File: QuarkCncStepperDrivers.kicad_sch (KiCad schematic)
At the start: 2 parts, among them J1 Conn_01x14, J2 Conn_01x14

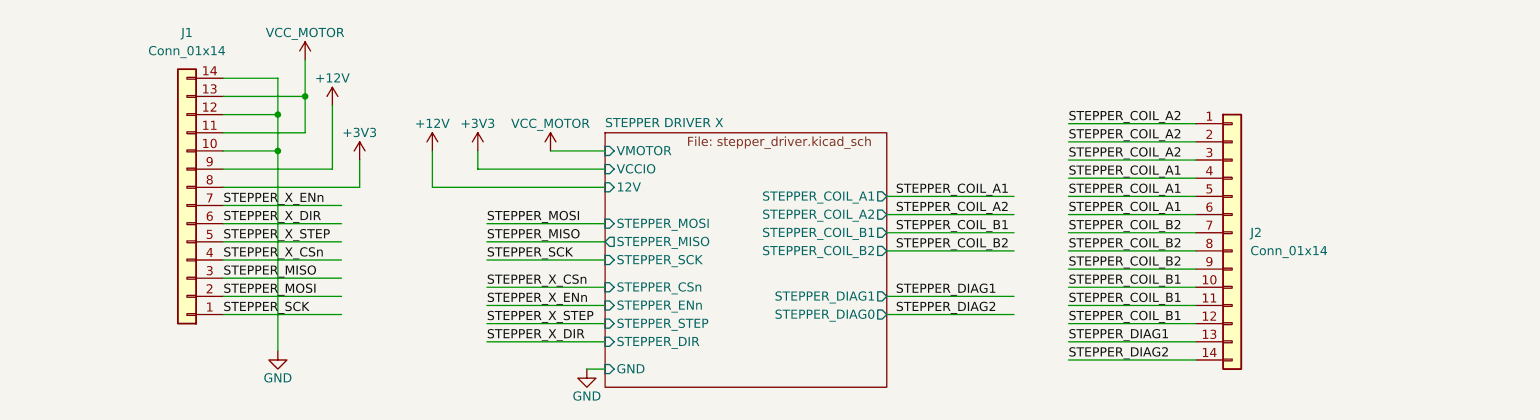
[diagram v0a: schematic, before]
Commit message: Removed 0Ohms. Keyed design
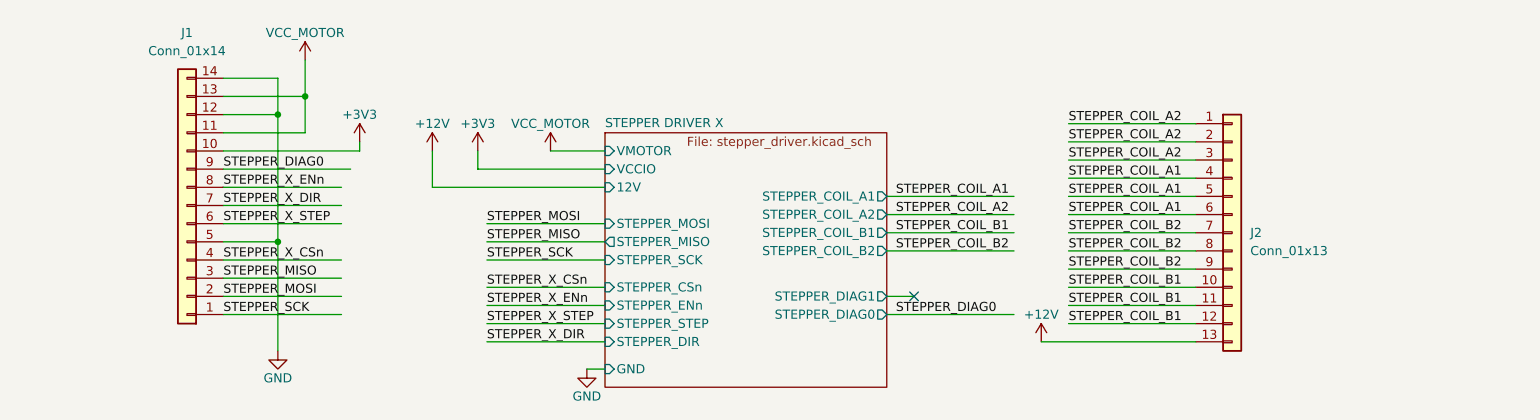
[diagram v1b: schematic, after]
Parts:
- J2: value Conn_01x14 -> Conn_01x13; footprint Connector_PinHeader_2.54mm:PinHeader_1x14_P2.54mm_Vertical -> Connector_PinHeader_2.54mm:PinHeader_1x13_P2.54mm_Vertical; symbol Connector_Generic:Conn_01x14 -> Connector_Generic:Conn_01x13; LCSC C2894937 -> C2894936
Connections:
- net STEPPER_DIAG1 is gone; now on net +12V: J2.13 (Pin_13)
- net +12V: no longer J1.9 (Pin_9)
- net +3V3: now also J1.10 (Pin_10); no longer J1.8 (Pin_8)
- net GND: now also J1.5 (Pin_5); no longer J1.10 (Pin_10)
- net STEPPER_X_DIR: now also J1.7 (Pin_7); no longer J1.6 (Pin_6)
- net STEPPER_X_ENn: now also J1.8 (Pin_8); no longer J1.7 (Pin_7)
- net STEPPER_X_STEP: now also J1.6 (Pin_6); no longer J1.5 (Pin_5)
- removed net STEPPER_DIAG2: J2.14 (Pin_14)
- new net STEPPER_DIAG0: J1.9 (Pin_9)
- no-connect marks 0 -> 1

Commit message: Updated pinout
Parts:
- removed J2: Conn_01x13, Connector_PinHeader_2.54mm:PinHeader_1x13_P2.54mm_Vertical, symbol Connector_Generic:Conn_01x13
- added J3: Conn_01x14, Connector_PinHeader_2.54mm:PinHeader_1x14_P2.54mm_Vertical, symbol Connector_Generic:Conn_01x14
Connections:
- net +12V: now also J1.9 (Pin_9)
- net STEPPER_COIL_A1: now also J3.4 (Pin_4), J3.5 (Pin_5), J3.6 (Pin_6)
- net STEPPER_COIL_A2: now also J3.1 (Pin_1), J3.2 (Pin_2), J3.3 (Pin_3)
- net STEPPER_COIL_B1: now also J3.10 (Pin_10), J3.11 (Pin_11), J3.12 (Pin_12)
- net STEPPER_COIL_B2: now also J3.7 (Pin_7), J3.8 (Pin_8), J3.9 (Pin_9)
- net STEPPER_DIAG0: now also J3.13 (Pin_13); no longer J1.9 (Pin_9)
- new net STEPPER_DIAG1: J3.14 (Pin_14)
- no-connect marks 1 -> 0
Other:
- note added: "Female Header on the left"
- note added: "Pin header on the right for keying"
- moved on the sheet: J1
